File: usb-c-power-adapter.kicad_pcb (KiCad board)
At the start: 4 copper layers, 21.9 x 52.5 mm, 124 parts, among them J1 USB-C_GCT_USB4105-GF-A, J2 JST_SH_1x4_SM04B-SRSS-TB-LF-SN, J3 JST_SH_1x4_SM04B-SRSS-TB-LF-SN, J4 Molex_Nano-Fit_1x2_105313-220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, Q1 SQS401EN-T1_BE3, U1 STUSB4500_QFN, U2 SIC477ED-T1-GE3, U3 AP62301Z6-7, U4 AP62301Z6-7, U5 TVS2200DRVR, U6 TPD4E02B04DQA, U7 TVS2200DRVR, U8 TVS2200DRVR

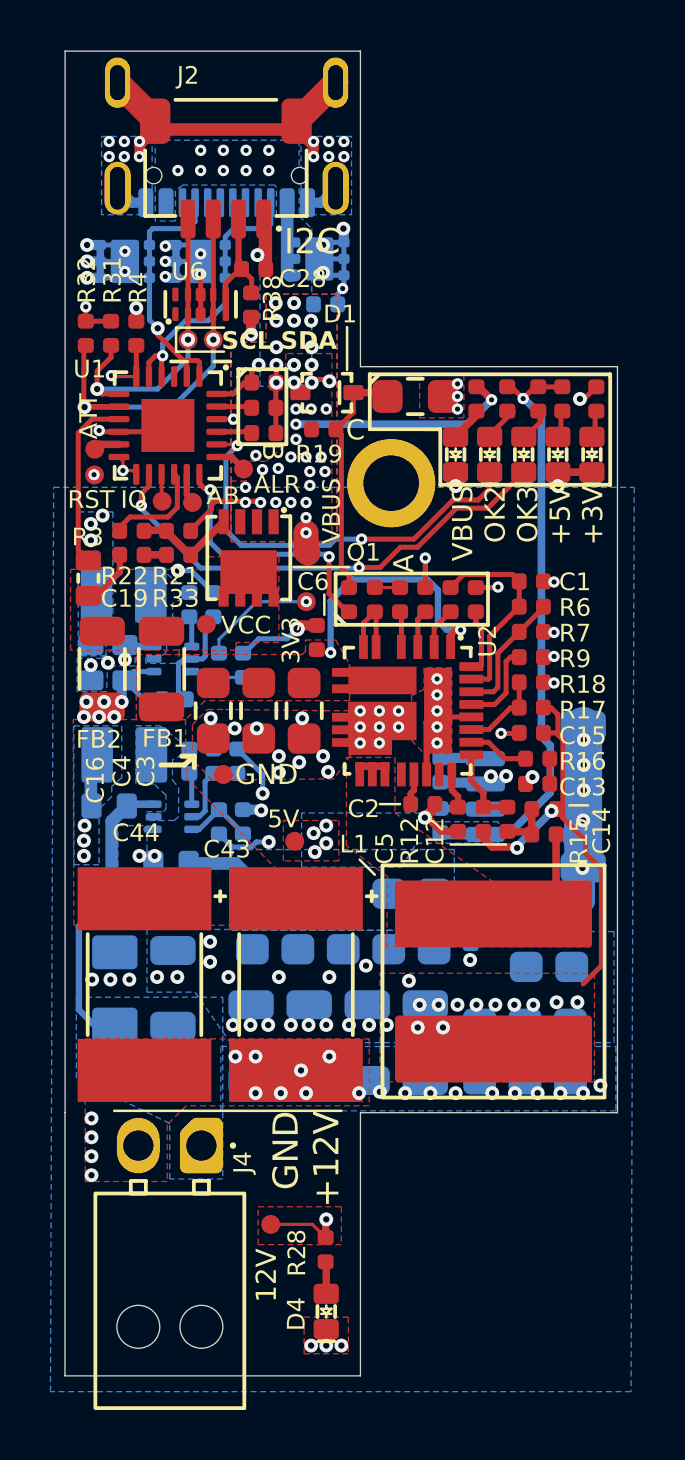
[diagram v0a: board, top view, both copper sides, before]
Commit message: [#79385] Replace molex on pcb
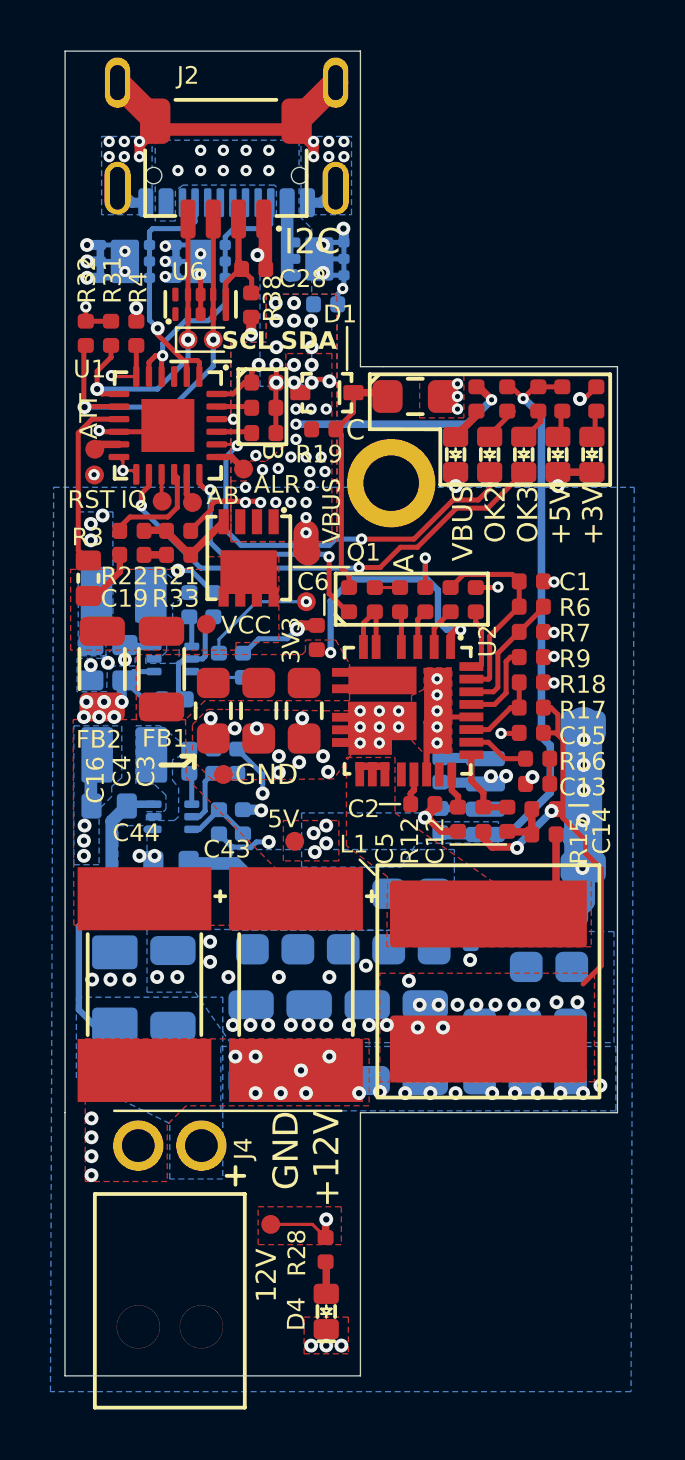
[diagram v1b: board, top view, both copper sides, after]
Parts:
- J4: value Molex_Nano-Fit_1x2_105313-2202_Horizontal -> Molex_Nano-Fit_1x2_1053131202; footprint antmicro-footprints:Conn_Molex_Nano-Fit_1x2_105313-2202_Horizontal -> antmicro-footprints:Conn_Molex_Nano-Fit_1x2_1053131102
- moved L1 0.20 mm to (98.3, 95.4)
- turned J4 to 0 degrees
